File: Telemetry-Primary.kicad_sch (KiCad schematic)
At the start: 43 parts, among them J1 CAN_LogicAnalyzer, J2 IMU_LogicAnalyzer, J3 GPS_LogicAnalyzer, J4 SWD, J5 SDCard_LogicAnalyzer, SW1 Reset, U1 STM32F429ZITx, Y1 8M, Y3 32.768k

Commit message: basic inputs
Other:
- note added: "2.1 - Removes the external RTC. There's no need to use an external RTC on the telemetry board. The microcontroller itself has an internal RTC that can be powered from the VBAT line and a 32.768kHz oscillator. Courtesy of Chase! 2.2 - New IO and Protection - Bluetooth, never actually tested please research - 4 buttons + 4 switches, HW debounced - SPI break out, choose best for layout - GPIO break 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"
- note removed: "2.1 - Removes the external RTC. There's no need to use an external RTC on the telemetry board. The microcontroller itself has an internal RTC that can be powered from the VBAT line and a 32.768kHz oscillator. Courtesy of Chase! 2.2 - New IO and Protection - Bluetooth, never actually tested please research - 4 buttons + 4 switches, hw debouncing - SPI break out, choose best for layout - GPIO break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"
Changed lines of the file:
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@@
     (fill (type none))
   )
-  (text "2.1 - Removes the external RTC.\n	There's no need to use an external RTC on the telemetry board. The microcontroller itself\n	has an internal RTC that can be powered from the VBAT line and a 32.768kHz oscillator. \n	Courtesy of Chase!\n\n2.2 - New IO and Protection\n	- Bluetooth, never actually tested please research\n	- 4 buttons + 4 switches, hw debouncing\n	- SPI break out, choose best for layout\n	- GPIO break out\n	- Power protection circuitry\n\nFuture Changes\n-Add keepout area around RTC clock (prevent noise), 8Mhz clock too?\n-Add impedance matching resistor to Ethernet line, consider all impedance matching\n-PR Checklist"
+  (text "2.1 - Removes the external RTC.\n	There's no need to use an external RTC on the telemetry board. The microcontroller itself\n	has an internal RTC that can be powered from the VBAT line and a 32.768kHz oscillator. \n	Courtesy of Chase!\n\n2.2 - New IO and Protection\n	- Bluetooth, never actually tested please research\n	- 4 buttons + 4 switches, HW debounced\n	- SPI break out, choose best for layout\n	- GPIO break out\n	- Power protection circuitry\n\nFuture Changes\n-Add keepout area around RTC clock (prevent noise), 8Mhz clock too?\n-Add impedance matching resistor to Ethernet line, consider all impedance matching\n-PR Checklist"
     (at 254 151.13 0)
     (effects (font (size 2 2) (thickness 0.4) bold) (justify left bottom))

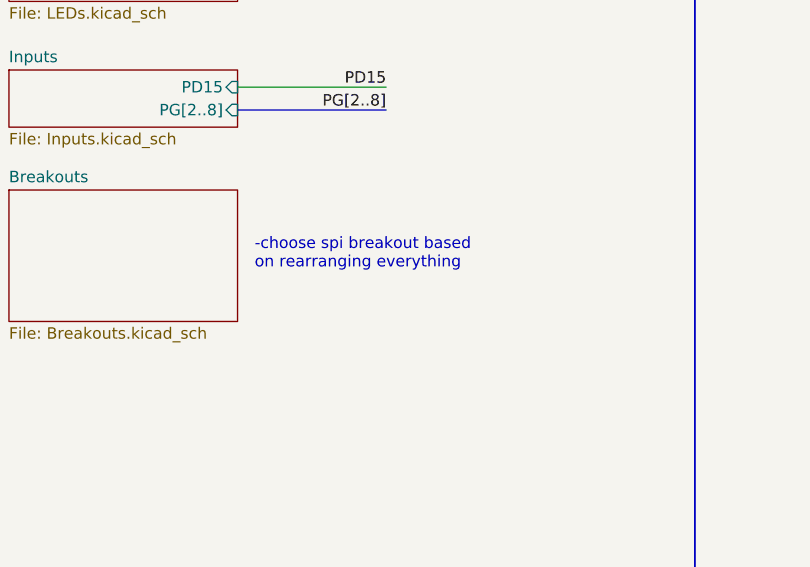
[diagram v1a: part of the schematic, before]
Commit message: switch changes, some caps, annotations
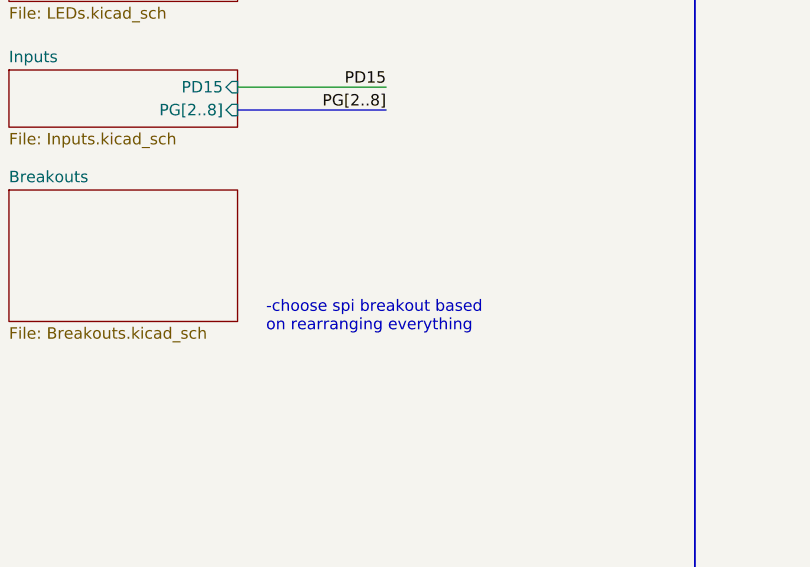
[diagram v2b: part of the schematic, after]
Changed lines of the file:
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@@
   )
   (text "-choose spi breakout based\non rearranging everything"
-    (at 44.45 229.235 0)
+    (at 45.72 236.22 0)
     (effects (font (size 1.27 1.27)) (justify left bottom))
   )

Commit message: layout rearranging
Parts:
- added C9: 4.7u, Capacitor_SMD:C_0805_2012Metric, symbol Device:C_Small
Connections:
- net +BATT: now also C9.1
- net GND: now also C9.2
- net PA11: no longer J3.5 (Pin_5)
- net PA8: no longer J3.4 (Pin_4)
- net PD7: now also J3.4 (Pin_4)
- net USART1_RX: no longer J3.3 (Pin_3)
- net USART1_TX: no longer J3.2 (Pin_2)
- net USART2_RX: now also J3.3 (Pin_3)
- net USART2_TX: now also J3.2 (Pin_2)
- net USART6_RX renamed PG9
- net PG9: now also J3.5 (Pin_5)
- net USART6_TX renamed PG14
- no-connect marks 63 -> 61
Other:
- added sheet Display (Breakouts.kicad_sch)
- note added: "1"
- note added: "109"
- note added: "2.1 - Removes the external RTC. There's no need to use an external RTC on the telemetry board. The microcontroller itself has an internal RTC that can be powered from the VBAT line and a 32.768kHz oscillator. Courtesy of Chase! 2.2 - New IO and Protection - Bluetooth - 4 buttons + 4 switches, HW debounced - SPI break out, choose best for layout - I2C/GPIO break out - Power protection circuitry Fu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"
- note added: "2xGPIO Breakout"
- note added: "37"
- note added: "73"
- note added: "Bluetooth"
- note added: "CAN"
- note added: "Display"
- note added: "Ethernet"
- note added: "Flashing Pins"
- note added: "GPS"
- note added: "IMU"
- note added: "Inputs"
- note added: "LEDs"
- note added: "Power Distribution"
- note added: "Questions: -ease of routing vs leds being on the same port -rtc batteries for both mcu and gps, are they necessary + asc regs say theyre allowed -fitting a display may be questionable with the space constaints -sensor discussions and what the new board needs to accommodate -spi breakout use pins or molex"
- note added: "SD Card"
- note added: "SPI Breakout"
- note added: "USB"
- note removed: "-choose spi breakout based on rearranging everything"
- note removed: "2.1 - Removes the external RTC. There's no need to use an external RTC on the telemetry board. The microcontroller itself has an internal RTC that can be powered from the VBAT line and a 32.768kHz oscillator. Courtesy of Chase! 2.2 - New IO and Protection - Bluetooth, never actually tested please research - 4 buttons + 4 switches, HW debounced - SPI break out, choose best for layout - GPIO break 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"
- moved on the sheet: C9

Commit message: breakout port
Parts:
- added J13: Breakouts, Connector_PinHeader_2.54mm:PinHeader_1x06_P2.54mm_Vertical, symbol Connector_Generic:Conn_01x06
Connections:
- net PD0: now also J13.5 (Pin_5)
- net PD1: now also J13.6 (Pin_6)
- net SPI3_CLK: now also J13.2 (Pin_2)
- net SPI3_CS: now also J13.1 (Pin_1)
- net SPI3_MISO: now also J13.3 (Pin_3)
- net SPI3_MOSI: now also J13.4 (Pin_4)
- no-connect marks 61 -> 55
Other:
- removed sheet Breakouts
- note added: "SPI Port + 2 GPIO"
- moved on the sheet: H1, H2, H3, H4

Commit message: led fix + notes
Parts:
- removed BT?: CR1220, Battery:BatteryHolder_Keystone_3000_1x12mm, symbol Device:Battery_Cell
- added J7: RTC_BATT, UTSVT_Connectors:Molex_MicroFit3.0_1x2xP3.00mm_PolarizingPeg_Vertical, symbol Connector_Generic:Conn_01x02
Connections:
- net PC7 is gone; now on net USART6_TX: U1.97 (PC7)
- net +BATT: now also J7.1 (Pin_1)
- net GND: now also J7.2 (Pin_2)
- net PC6 renamed USART6_TX
- no-connect marks 55 -> 56
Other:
- sheet GPS ports: added BATT; removed none
- sheet LEDs ports: added PE[7..9], PF[11..15]; removed PE[7..15]
- note added: "-MICROFIT FOR BREAKOUT -TRY GROUPING TEST PINS -move antenna/gps to bottom left maybe ???"
- note removed: "Questions: -ease of routing vs leds being on the same port -rtc batteries for both mcu and gps, are they necessary + asc regs say theyre allowed -fitting a display may be questionable with the space constaints -sensor discussions and what the new board needs to accommodate -spi breakout use pins or molex"
- moved on the sheet: J3, J5

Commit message: layout changes, telemetryCAN added, IMU removed
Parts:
- removed J2: IMU_LogicAnalyzer, Connector_PinHeader_2.54mm:PinHeader_1x05_P2.54mm_Vertical, symbol Connector_Generic:Conn_01x05
- removed R? (x2): 4.7k, Resistor_SMD:R_0805_2012Metric, symbol Device:R
- added J2: CAN_LogicAnalyzer, Connector_PinHeader_2.54mm:PinHeader_1x03_P2.54mm_Vertical, symbol Connector_Generic:Conn_01x03
- J13: footprint Connector_PinHeader_2.54mm:PinHeader_1x06_P2.54mm_Vertical -> Connector_Molex:Molex_Micro-Fit_3.0_43045-0612_2x03_P3.00mm_Vertical; P/N 10129378-910001BLF -> 43045-0612
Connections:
- net GND: now also J2.1 (Pin_1)
- net PD0: now also J13.3 (Pin_3); no longer J13.5 (Pin_5)
- net PD10: now also J3.4 (Pin_4)
- net PD11: now also J3.5 (Pin_5)
- net PD7: no longer J3.4 (Pin_4)
- net PG9: no longer J3.5 (Pin_5)
- net SPI3_CLK: now also J13.4 (Pin_4); no longer J13.2 (Pin_2)
- net SPI3_MISO: now also J13.2 (Pin_2); no longer J13.3 (Pin_3)
- net SPI3_MOSI: now also J13.5 (Pin_5); no longer J13.4 (Pin_4)
- net USART2_RX: no longer J3.3 (Pin_3)
- net USART2_TX: no longer J3.2 (Pin_2)
- net USART3_RX: now also J3.3 (Pin_3)
- net USART3_TX: now also J3.2 (Pin_2)
- net USART6_TX: no longer U1.97 (PC7)
- net I2C1_SCL renamed CAN2_TX
- net CAN2_TX: now also J2.2 (Pin_2)
- net I2C1_SDA renamed PB7
- net PB5 renamed CAN2_RX
- net CAN2_RX: now also J2.3 (Pin_3)
- new net USART6_RX: U1.97 (PC7)
- no-connect marks 56 -> 57
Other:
- sheet CAN renamed CarCAN
- removed sheet Display
- removed sheet IMU
- added sheet TelemetryCAN (TelemetryCAN.kicad_sch)
- sheet CarCAN: file CAN.kicad_sch -> CarCAN.kicad_sch
- note added: "2.1 - Removes the external RTC. There's no need to use an external RTC on the telemetry board. The microcontroller itself has an internal RTC that can be powered from the VBAT line and a 32.768kHz oscillator. Courtesy of Chase! 3.0 - New IO and Protection - Bluetooth - 4 buttons + 4 switches, HW debounced - SPI breakout - 2x GPIO breakout - Power protection circuitry - Better layout grouping - RT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"
- note added: "CarCAN"
- note added: "TelemetryCAN"
- note removed: "-MICROFIT FOR BREAKOUT -TRY GROUPING TEST PINS -move antenna/gps to bottom left maybe ???"
- note removed: "2.1 - Removes the external RTC. There's no need to use an external RTC on the telemetry board. The microcontroller itself has an internal RTC that can be powered from the VBAT line and a 32.768kHz oscillator. Courtesy of Chase! 2.2 - New IO and Protection - Bluetooth - 4 buttons + 4 switches, HW debounced - SPI break out, choose best for layout - I2C/GPIO break out - Power protection circuitry Fu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"
- note removed: "Addr: 0x28"
- note removed: "CAN"
- note removed: "Display"
- note removed: "IMU"

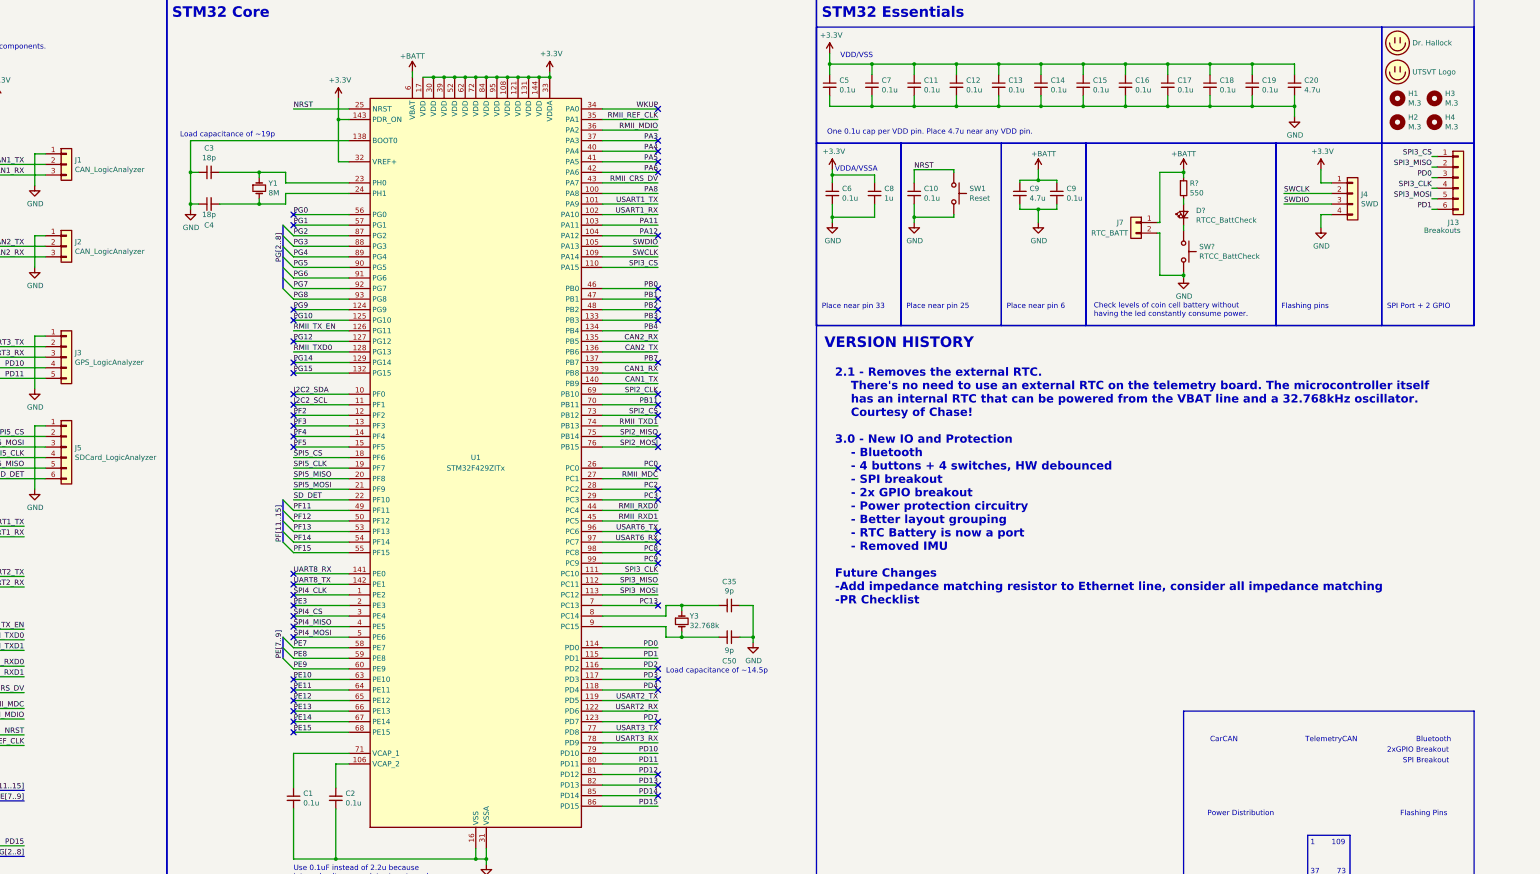
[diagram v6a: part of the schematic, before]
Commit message: inputs routing + fixed models + clock keepouts
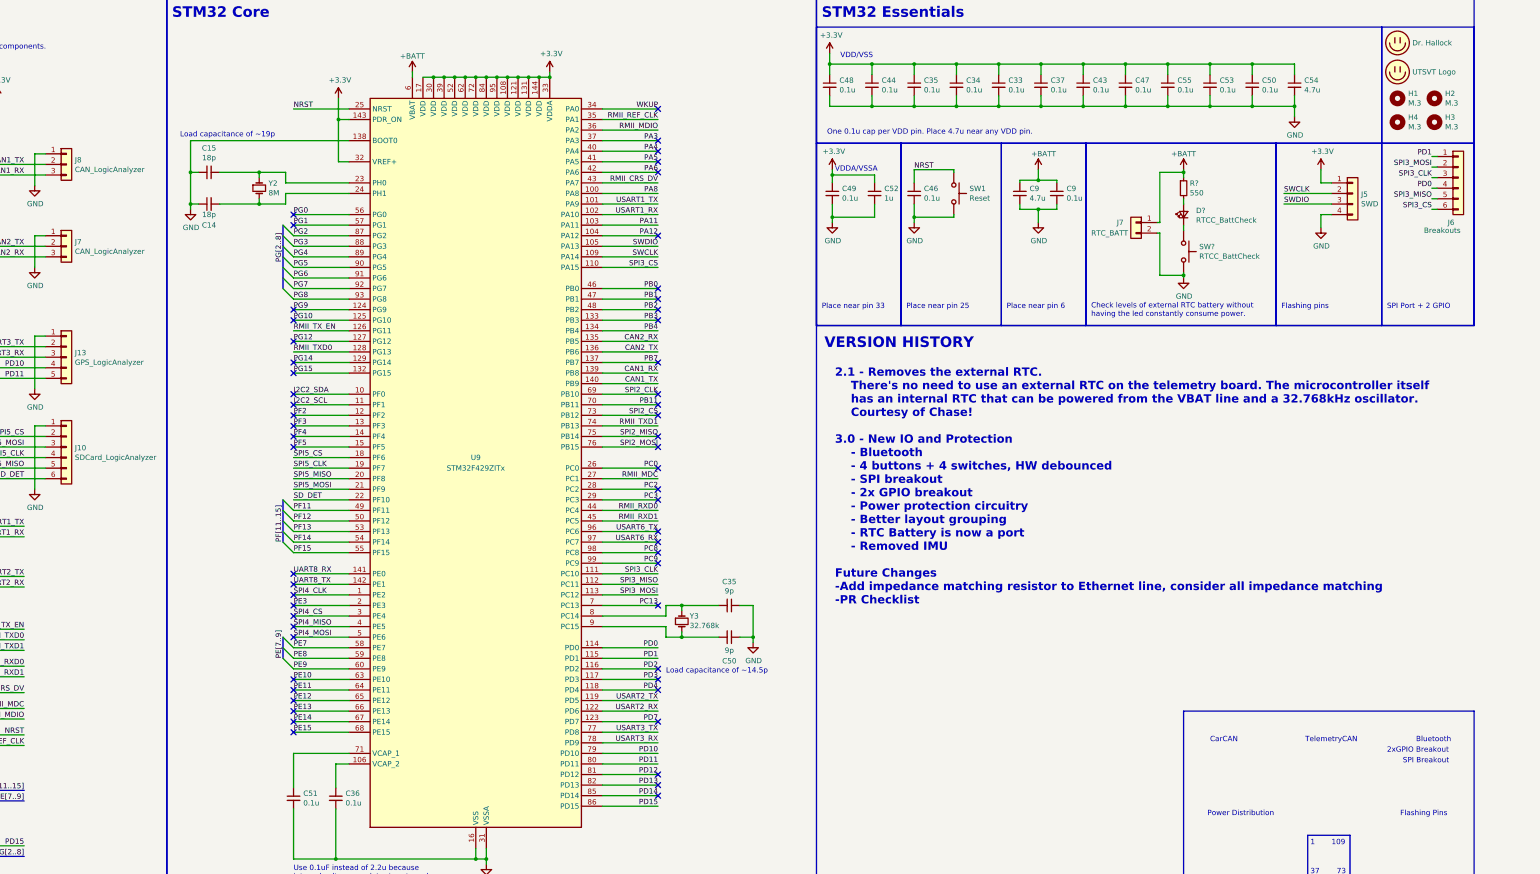
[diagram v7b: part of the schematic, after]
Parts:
- renumbered C4 to C14, C3 to C15, C13 to C33, C12 to C34, C11 to C35, C2 to C36, C14 to C37, C15 to C43, C7 to C44, C10 to C46, C16 to C47, C5 to C48, C6 to C49, C19 to C50, C1 to C51, C8 to C52, C18 to C53, C20 to C54, C17 to C55, H3 to H2, H4 to H3, H2 to H4, J5 to J10, J3 to J13, J4 to J5, J13 to J6, J2 to J7, J1 to J8, LOGO2 to LOGO1, LOGO1 to LOGO2, U1 to U9, Y1 to Y2
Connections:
- net PD0: now also J6.4 (Pin_4); no longer J6.3 (Pin_3)
- net PD1: now also J6.1 (Pin_1); no longer J6.6 (Pin_6)
- net SPI3_CLK: now also J6.3 (Pin_3); no longer J6.4 (Pin_4)
- net SPI3_CS: now also J6.6 (Pin_6); no longer J6.1 (Pin_1)
- net SPI3_MISO: now also J6.5 (Pin_5); no longer J6.2 (Pin_2)
- net SPI3_MOSI: now also J6.2 (Pin_2); no longer J6.5 (Pin_5)
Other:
- note added: "Check levels of external RTC battery without having the led constantly consume power."
- note removed: "Check levels of coin cell battery without having the led constantly consume power."

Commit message: silk screen cleanup + comments
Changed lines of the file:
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@@
     (effects (font (size 1.27 1.27)) (justify left bottom))
   )
-  (text "2.1 - Removes the external RTC.\n	There's no need to use an external RTC on the telemetry board. The microcontroller itself\n	has an internal RTC that can be powered from the VBAT line and a 32.768kHz oscillator. \n	Courtesy of Chase!\n\n3.0 - New IO and Protection\n	- Bluetooth\n	- 4 buttons + 4 switches, HW debounced\n	- SPI breakout\n	- 2x GPIO breakout\n	- Power protection circuitry\n	- Better layout grouping\n	- RTC Battery is now a port\n	- Removed IMU\n\nFuture Changes\n-Add impedance matching resistor to Ethernet line, consider all impedance matching\n-PR Checklist"
-    (at 254 158.115 0)
+  (text "2.1 - Removes the external RTC.\n	There's no need to use an external RTC on the telemetry board. The microcontroller itself\n	has an internal RTC that can be powered from the VBAT line and a 32.768kHz oscillator. \n	Courtesy of Chase!\n\n3.0 - New IO and Protection\n	- Bluetooth\n	- 4 buttons + 4 switches, HW debounced\n	- SPI breakout\n	- 2x GPIO breakout\n	- Power protection circuitry\n	- Better layout grouping\n	- RTC Battery is now a port\n	- Removed IMU\n\nFuture Changes\n-Add impedance matching resistor to Ethernet line, SPI, gps antenna\n-Consider antenna placement and interferance, separate ground ???\n-move flashing pins to edge and drop down right side\n-PR Checklist"
+    (at 254 163.195 0)
     (effects (font (size 2 2) (thickness 0.4) bold) (justify left bottom))
   )
